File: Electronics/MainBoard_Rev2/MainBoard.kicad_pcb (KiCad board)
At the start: 2 copper layers, 57.2 x 35.1 mm, 65 parts, among them J1 Conn_01x04_Female, J10 USB_B_Micro, J2 DB9_Female, Q30 PMBT2222A, Q35 PMBT2222A, U1 ESP32-WROOM-32, U10 FT230XS, U50 MCP73832-2-OT, U51 SPX3819M5-L-3-3

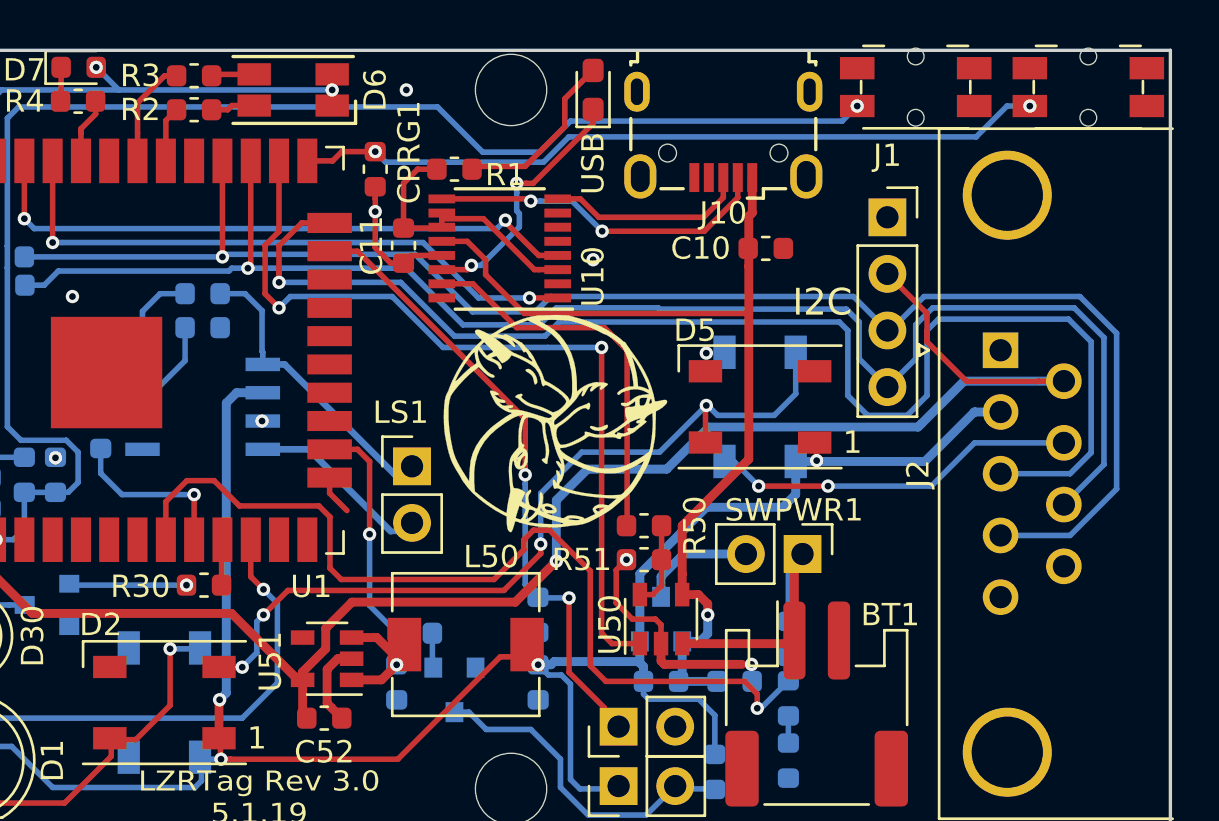
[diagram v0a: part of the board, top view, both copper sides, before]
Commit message: Last few tweaks, i.e. fixing ground plane
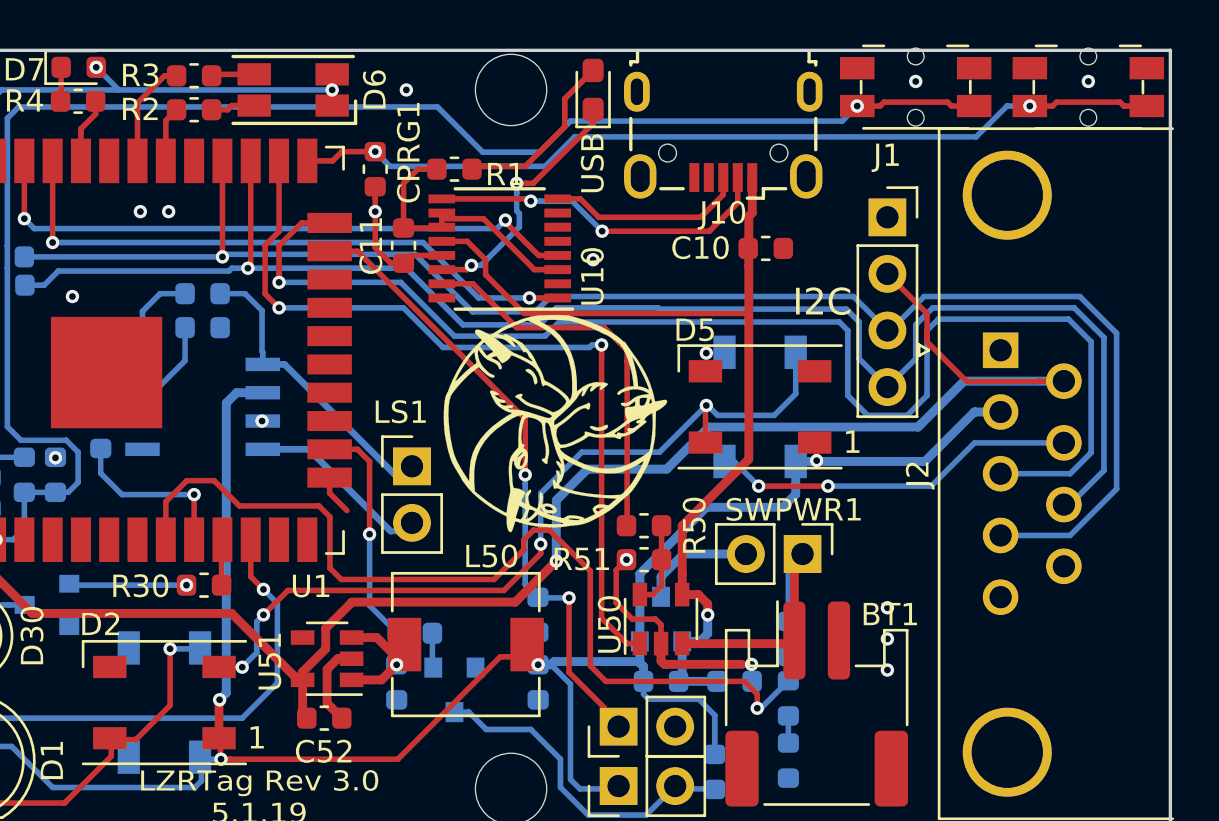
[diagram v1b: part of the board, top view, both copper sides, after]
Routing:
- net /GPIO0: track 33.8 -> 39.4 mm
- net /RESET: track 64.6 -> 70.0 mm
- net /CHG_STAT: track 37.5 -> 36.8 mm
- net GND: vias 9 -> 16

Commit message: Began reworking a few PCB elements
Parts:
- removed AMP1: TPA301, Package_SO:SOIC-8_3.9x4.9mm_P1.27mm
- removed C38, C39, CPRG1: 150nF, Capacitor_SMD:C_0603_1608Metric
- removed LS1: Speaker, Connector_PinHeader_2.54mm:PinHeader_1x02_P2.54mm_Vertical
- removed R38: 10k, Resistor_SMD:R_0603_1608Metric
- removed R39: 20k-50k, Resistor_SMD:R_0603_1608Metric
- R1: value 2.2k -> 220
- R2, R3: value 2.2k -> 220R
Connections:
- net Net-(U1-Pad13) renamed /LRCLK
- net Net-(U1-Pad8) renamed /BCLK
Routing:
- net +BATT: track 98.8 -> 81.8 mm, vias 4 -> 3
- net Net-(AMP1-Pad5): track 13.4 -> 0.00 mm
- net Net-(AMP1-Pad8): track 8.22 -> 0.00 mm
- net /AUDIO: track 7.73 -> 0.00 mm, vias 1 -> 0
- net Net-(AMP1-Pad4): track 6.51 -> 0.00 mm
- net Net-(AMP1-Pad2): track 5.26 -> 0.00 mm
- net Net-(C38-Pad1): track 1.47 -> 0.00 mm

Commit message: Began rework to even better hardware
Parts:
- removed D1: WS2812B_5mm, LED_THT:LED_D5.0mm-4_RGB
- removed L50: 100uH, Inductor_SMD:L_6.3x6.3_H3
- removed R50: 2.2k, Resistor_SMD:R_0603_1608Metric
- removed R51: 10k, Resistor_SMD:R_0603_1608Metric
- added C53: 10uF, Capacitor_SMD:C_0805_2012Metric, F.Cu at (131.8, 120.1)
- added C54: 1uF, Capacitor_SMD:C_0805_2012Metric, F.Cu at (131.8, 118.1)
- added L1: 445-3654-1-ND, Inductor_SMD:L_1210_3225Metric, F.Cu at (127.8, 118.7)
- added U3: LSM6DS3, Package_LGA:LGA-14_3x2.5mm_P0.5mm_LayoutBorder3x4y, F.Cu at (138.8, 118.7)
- U50: value MCP73832-2-OT -> AP2114H-3_3TRG1
- U51: value SPX3819M5-L-3-3 -> LP3947; footprint Package_TO_SOT_SMD:SOT-23-5 -> Package_SON:WSON-14-1EP_4.0x4.0mm_P0.5mm_EP2.6x2.6mm
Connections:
- J1 pad 3: /SCL -> SCL
- J1 pad 4: /SDA -> SDA
- J2 pad 4: /SCL -> SCL
- J2 pad 8: /SDA -> SDA
- R5 pad 2: /SCL -> SCL
- R6 pad 2: /SDA -> SDA
- U1 pad 27: /SDA -> SDA
- U1 pad 28: /SCL -> SCL
- U50 pad 1: /CHG_STAT -> GND
- U50 pad 2: GND -> +3V3
- U50 pad 3: /PowerHandling/B_Raw+ -> Net-(C51-Pad1)
- U50 pad 4: /USB Connection/+5V_USB -> +3V3
- U50 pad 5: Net-(R50-Pad2) -> (no net)
- U51 pad 1: Net-(C51-Pad1) -> Net-(U51-Pad1)
- U51 pad 2: GND -> SCL
- U51 pad 3: Net-(C51-Pad1) -> SDA
- U51 pad 4: Net-(U51-Pad4) -> /PowerHandling/B_Raw+
- U51 pad 5: +3V3 -> Net-(U51-Pad5)
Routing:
- net SCL: track 0.00 -> 69.7 mm, vias 0 -> 1
- net /SCL: track 69.7 -> 0.00 mm, vias 1 -> 0
- net SDA: track 0.00 -> 68.5 mm, vias 0 -> 1
- net /SDA: track 68.5 -> 0.00 mm, vias 1 -> 0
- net GND: track 22.0 -> 11.7 mm, vias 16 -> 14
- net +3V3: track 113.1 -> 123.4 mm, vias 4 -> 6
- net Net-(R50-Pad2): track 3.89 -> 0.00 mm
- net (no net): track 0.00 -> 3.89 mm

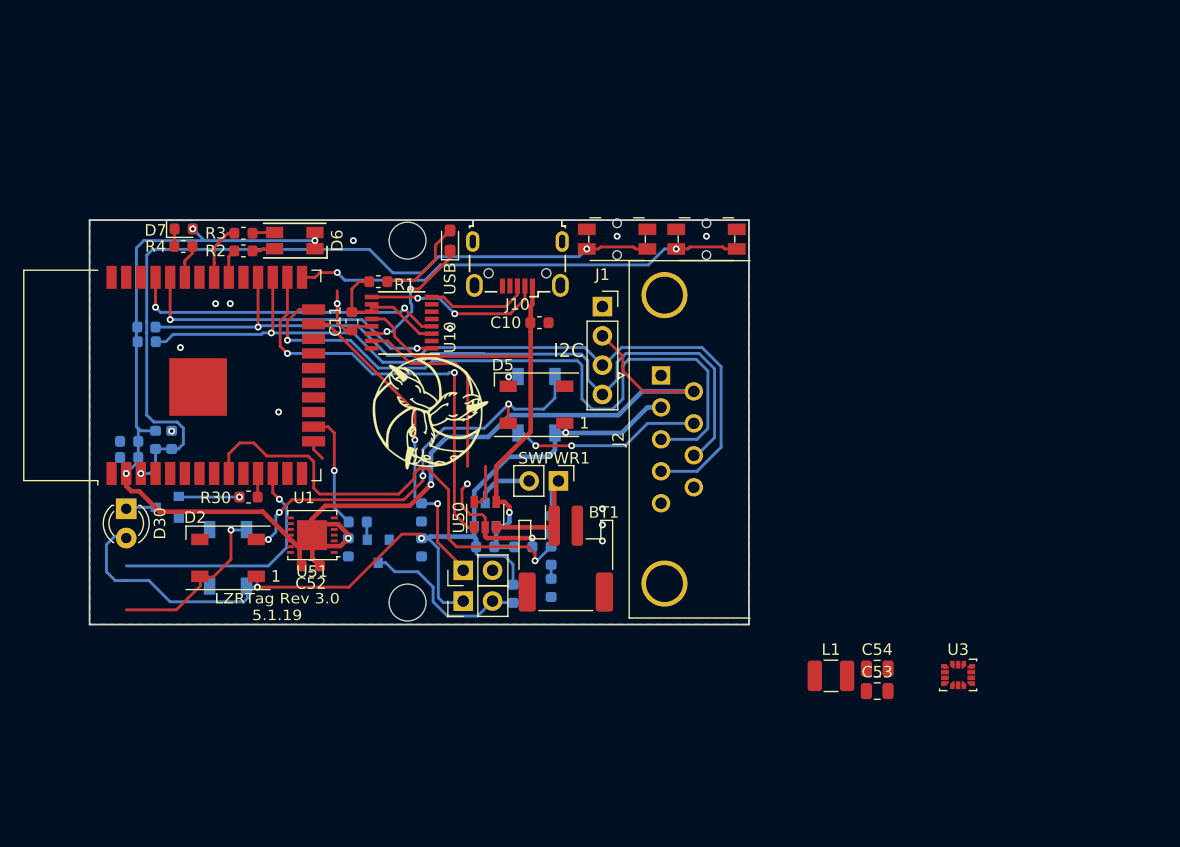
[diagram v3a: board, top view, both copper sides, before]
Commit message: Fixed footprint assignment
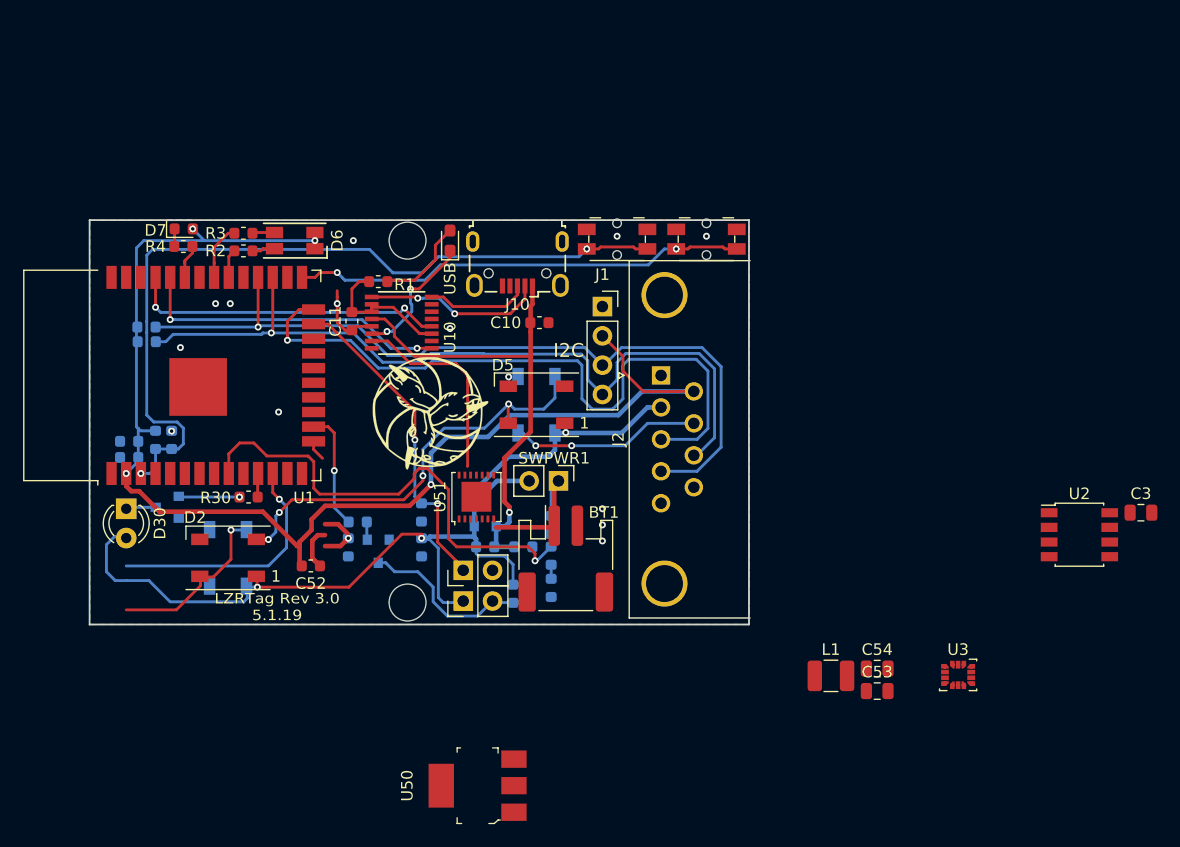
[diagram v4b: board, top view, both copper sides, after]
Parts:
- added C3: 0.1uF, Capacitor_SMD:C_0805_2012Metric, F.Cu at (154.6, 104.6)
- added U2: WS2811, Package_SO:SSOP-8_3.95x5.21x3.27mm_P1.27mm, F.Cu at (149.3, 106.5)
- U50: footprint Package_TO_SOT_SMD:SOT-23-5 -> digikey-footprints:SOT-223
- moved U50 23.5 mm to (97.1, 128.3)
- moved U51 14.6 mm to (97.0, 103.3), turned to 90 degrees
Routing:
- net /CHG_STAT: track 36.8 -> 0.00 mm, vias 2 -> 0
- net +3V3: track 123.4 -> 113.1 mm, vias 6 -> 4
- net (no net): track 3.89 -> 0.00 mm
- net /USB Connection/+5V_USB: track 43.1 -> 42.0 mm

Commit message: MORE
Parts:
- removed C10: 10uF, Capacitor_SMD:C_0603_1608Metric
- removed C11, CRST1: 150nF, Capacitor_SMD:C_0603_1608Metric
- removed J10: USB_B_Micro, Connector_USB:USB_Micro-B_Wuerth_629105150521
- removed R1: 220, Resistor_SMD:R_0603_1608Metric
- removed RRST1: R_Small, Resistor_SMD:R_0603_1608Metric
- removed SWPRG1, SWRST1: SW_Push, Button_Switch_SMD:Panasonic_EVQPUL_EVQPUC
- removed U10: FT230XS, Package_SO:SSOP-16_3.9x4.9mm_P0.635mm
- added C19: 100nF, Capacitor_SMD:C_0805_2012Metric, F.Cu at (113.8, 68.8)
- added C8: 150nF, Capacitor_SMD:C_0805_2012Metric, F.Cu at (96.4, 88.8)
- added C9: 10uF, Capacitor_SMD:C_0805_2012Metric, F.Cu at (110.6, 74.2)
- added J3: USB_B_Micro, Connector_USB:USB_Micro-B_Wuerth_629105150521, F.Cu at (100.6, 83.0)
- added Q5: Q_NPN_BEC, Package_TO_SOT_SMD:SOT-23, F.Cu at (100.4, 73.9)
- added Q6: Q_NPN_BEC, Package_TO_SOT_SMD:SOT-23, F.Cu at (96.9, 73.9)
- added R12: 220, Resistor_SMD:R_0805_2012Metric, F.Cu at (113.8, 66.8)
- added R13: R_Small, Resistor_SMD:R_0805_2012Metric, F.Cu at (107.2, 74.2)
- added R14: R_Small, Resistor_SMD:R_0805_2012Metric, F.Cu at (113.8, 64.9)
- added R15: R_Small, Resistor_SMD:R_0805_2012Metric, F.Cu at (103.8, 74.2)
- added U13: FT231XS, Package_SO:SSOP-20_3.9x8.7mm_P0.635mm, F.Cu at (91.1, 88.9)
- C51: moved to F.Cu
- DUSB1: footprint LED_SMD:LED_0603_1608Metric_Pad1.05x0.95mm_HandSolder -> LED_SMD:LED_0805_2012Metric
- moved L1 42.7 mm to (85.7, 111.6)
- moved U50 26.5 mm to (87.5, 103.6), turned to 0 degrees
- moved C51 3.90 mm to (82.7, 109.8)
- moved C52 1.65 mm to (81.1, 109.8), turned to 270 degrees
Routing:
- net /GPIO0: track 39.4 -> 3.22 mm, vias 2 -> 0
- net /RESET: track 70.0 -> 44.1 mm, vias 2 -> 1
- net /USB Connection/Charge_EN: track 17.4 -> 0.00 mm
- net Net-(J3-Pad2): track 0.00 -> 16.6 mm
- net Net-(J10-Pad2): track 15.5 -> 0.00 mm, vias 2 -> 0
- net Net-(DUSB1-Pad1): track 11.4 -> 0.00 mm, vias 2 -> 0
- net Net-(J3-Pad3): track 0.00 -> 11.2 mm
- net GND: track 11.7 -> 1.80 mm, vias 14 -> 10
- net Net-(J10-Pad3): track 8.96 -> 0.00 mm
- net Net-(DUSB1-Pad2): track 8.01 -> 0.00 mm
- net Net-(C51-Pad1): track 4.66 -> 11.2 mm, vias 1 -> 0
- net /E>U: track 27.6 -> 22.3 mm
- net /USB Connection/USB3.3: track 12.3 -> 9.09 mm
- net /USB Connection/+5V_USB: track 42.0 -> 43.9 mm
- net +BATT: track 81.8 -> 82.9 mm, vias 3 -> 4
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
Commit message: Temporary polishing of PCB
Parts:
- removed R57: 100k, Resistor_SMD:R_0603_1608Metric
- removed U2: WS2811, Package_SO:SSOP-8_3.95x5.21x3.27mm_P1.27mm
- removed U51: LP3947, Package_SON:WSON-14-1EP_4.0x4.0mm_P0.5mm_EP2.6x2.6mm
- added AMP1: MAX98357A, Package_DFN_QFN:QFN-16-1EP_3x3mm_P0.5mm_EP2.7x2.7mm_ThermalVias, B.Cu at (78.1, 95.7)
- added C4: 10uF, Capacitor_SMD:C_0805_2012Metric, B.Cu at (73.6, 94.5)
- added D1: COM-12999, digikey-footprints:LED_RGB_WP154A4SUREQBFZGC, F.Cu at (66.6, 111.2)
- added U4: MAX1555EZK_T, digikey-footprints:SOT-753, F.Cu at (97.5, 104.5)
- C1, C2, C31, C50: footprint Capacitor_SMD:C_0603_1608Metric -> Capacitor_SMD:C_0805_2012Metric
- C19, C3, C53, C8, C9, L1, Q6, R12, R14, R15, U3: moved to B.Cu
- C51, C52: footprint Capacitor_SMD:C_0603_1608Metric -> Capacitor_SMD:C_0805_2012Metric; moved to B.Cu
- R2, R3, R30, R35, R4, R5, R52, R55, R6: footprint Resistor_SMD:R_0603_1608Metric -> Resistor_SMD:R_0805_2012Metric
- R56: value 100k -> 200k; footprint Resistor_SMD:R_0603_1608Metric -> Resistor_SMD:R_0805_2012Metric
- moved C3 81.9 mm to (73.6, 92.4)
- moved U3 66.7 mm to (77.8, 91.6), turned to 180 degrees
- moved C19 53.4 mm to (70.4, 99.8)
- moved R15 41.0 mm to (70.4, 97.9)
- moved C54 37.9 mm to (98.2, 100.6), turned to 180 degrees
- moved C53 33.0 mm to (102.1, 105.5)
- moved R14 32.1 mm to (89.2, 85.3), turned to 270 degrees
- moved R12 25.6 mm to (94.7, 83.9), turned to 90 degrees
- moved R13 25.1 mm to (85.6, 86.9), turned to 270 degrees
- moved C9 20.7 mm to (96.3, 89.2), turned to 180 degrees
- moved Q5 17.0 mm to (86.4, 83.4), turned to 90 degrees
- moved Q6 15.2 mm to (86.2, 84.7), turned to 180 degrees
- moved R56 2.07 mm to (104.9, 109.9)
- moved C8 1.65 mm to (96.3, 87.2)
- moved R55 1.53 mm to (104.9, 106.3)
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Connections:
- R56 pad 2: Net-(R56-Pad2) -> GND
- U50 pad 4: +3V3 -> Net-(U50-Pad4)
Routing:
- net /CHG_STAT: track 0.00 -> 36.4 mm, vias 0 -> 2
- net GND: track 1.80 -> 26.8 mm, vias 10 -> 16
- net +BATT: track 82.9 -> 107.2 mm, vias 4 -> 2
- net +3V3: track 112.1 -> 130.0 mm, vias 4 -> 7
- net Net-(DUSB1-Pad1): track 0.00 -> 10.7 mm, vias 0 -> 2
- net /USB Connection/+5V_USB: track 43.9 -> 50.9 mm, vias 1 -> 2
- net /RESET: track 44.1 -> 37.4 mm
- net /BCLK: track 0.00 -> 6.49 mm, vias 0 -> 1
- net /LRCLK: track 0.00 -> 5.45 mm, vias 0 -> 1
- net /AUDIO: track 0.00 -> 5.05 mm, vias 0 -> 1
- net Net-(Q6-Pad2): track 0.00 -> 4.66 mm, vias 0 -> 1
- net /USB Connection/USB3.3: track 9.09 -> 13.5 mm, vias 0 -> 1
- net Net-(DUSB1-Pad2): track 0.00 -> 2.92 mm, vias 0 -> 1
- net Net-(Q5-Pad2): track 0.00 -> 2.90 mm, vias 0 -> 1
- net /V_SENSE: track 42.2 -> 39.6 mm
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- added copper zone on F.Cu, net /PowerHandling/B_Raw+

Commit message: Began reworking sections
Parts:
- removed C1: 10uF, Capacitor_SMD:C_0805_2012Metric
- removed C51: 150nF, Capacitor_SMD:C_0805_2012Metric
- removed L1: 445-3654-1-ND, Inductor_SMD:L_1210_3225Metric
- added C5: 47uF, Capacitor_SMD:C_1206_3216Metric, B.Cu at (67.5, 95.5)
- added D8: D_Zener_ALT, Diode_SMD:D_SOD-123F, B.Cu at (95.0, 99.9)
- added J4: Conn_01x04_Male, MainBoard_Rev2:nav_switch_COM_08184, B.Cu at (71.6, 81.4)
- added R1: 220, Resistor_SMD:R_0805_2012Metric, F.Cu at (107.5, 98.8)
- added R7: 220, Resistor_SMD:R_0805_2012Metric, B.Cu at (118.0, 95.4)
- added TP1: TestPoint, TestPoint:TestPoint_Pad_2.0x2.0mm, B.Cu at (80.6, 101.2)
- added TP2: TestPoint, TestPoint:TestPoint_Pad_2.0x2.0mm, B.Cu at (74.3, 101.2)
- added TP3: TestPoint, TestPoint:TestPoint_Pad_2.0x2.0mm, B.Cu at (77.5, 101.2)
- C50: value 10uF -> 1uF
- moved U50 6.38 mm to (83.8, 108.7)
- moved H5 6.34 mm to (87.2, 97.0)
- moved C52 4.57 mm to (83.5, 106.2)
- moved H6 4.04 mm to (90.6, 99.3)
- moved C54 0.60 mm to (98.4, 100.0), turned to 90 degrees
- moved C4 0.51 mm to (73.6, 95.0)
- moved H3 0.46 mm to (109.4, 106.2)
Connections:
- AMP1 pad 7: +BATT -> Net-(AMP1-Pad7)
- J2 pad 3: /IR_IN -> Net-(J2-Pad3)
- J2 pad 7: /LED_2 -> Net-(J2-Pad7)
- U1 pad 29: Net-(U1-Pad29) -> /CTRL_BACK
- U1 pad 36: Net-(U1-Pad36) -> /CTRL_FWD
- U1 pad 37: Net-(U1-Pad37) -> /CTRL_DOWN
- U50 pad 2: +3V3 -> Net-(U50-Pad2)
- U50 pad 3: Net-(C51-Pad1) -> +BATT
- U50 pad 4: Net-(U50-Pad4) -> +3V3
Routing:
- net /LED_2: track 16.5 -> 6.35 mm, vias 2 -> 1
- net Net-(C51-Pad1): track 8.66 -> 0.00 mm, vias 1 -> 0
- net Net-(J2-Pad7): track 0.00 -> 8.27 mm, vias 0 -> 1
- net /IR_IN: track 58.9 -> 52.2 mm
- net Net-(J2-Pad3): track 0.00 -> 6.21 mm
- net /CTRL_DOWN: track 0.00 -> 4.06 mm, vias 0 -> 1
- net SCL: track 71.9 -> 75.0 mm
- net SDA: track 70.2 -> 73.2 mm
- net /CTRL_BACK: track 0.00 -> 3.00 mm, vias 0 -> 1
- net /RESET: track 37.4 -> 40.3 mm
- net /TRIGGER: track 29.8 -> 27.4 mm
- net /USB Connection/+5V_USB: track 50.9 -> 49.0 mm
- net /CTRL_FWD: track 0.00 -> 1.77 mm, vias 0 -> 1
- net +3V3: track 130.0 -> 129.1 mm
- net GND: track 26.8 -> 26.2 mm, vias 16 -> 13
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
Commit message: Continued work on the current electronics
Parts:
- removed H5: MountingHole, MainBoard_Rev2:QR_Link
- added J5: Conn_01x02_Male, Connector_PinHeader_2.00mm:PinHeader_1x02_P2.00mm_Vertical, F.Cu at (85.7, 95.1)
- added R8: 220, Resistor_SMD:R_0805_2012Metric, B.Cu at (118.3, 98.5)
- added R9: 220, Resistor_SMD:R_0805_2012Metric, B.Cu at (118.5, 101.1)
- moved H6 0.70 mm to (90.8, 99.9)
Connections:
- J2 pad 4: SCL -> Net-(J2-Pad4)
- J2 pad 8: SDA -> Net-(J2-Pad8)
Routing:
- net Net-(AMP1-Pad9): track 0.00 -> 6.86 mm
- net Net-(AMP1-Pad10): track 0.00 -> 6.24 mm
- net SCL: track 75.0 -> 69.3 mm
- net Net-(J2-Pad4): track 0.00 -> 5.10 mm
- net SDA: track 73.2 -> 69.0 mm
- net GND: track 26.2 -> 28.9 mm
- net Net-(J2-Pad8): track 0.00 -> 1.98 mm
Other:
- board text added: "Follow me on HackADay: bit.ly/XASLZR"
- board text added: "LZRTag HW 3.2 30.08.2019"
- board text removed: "Follow me on HackADay:"
- board text removed: "LZRTag Rev 3.0 5.1.19"
